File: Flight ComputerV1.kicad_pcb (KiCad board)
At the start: 4 copper layers, 100 x 100 mm, 37 parts, among them J101 ICSP, J102 Screw_Terminal_01x02, J103 Conn_01x08, J104 Conn_01x07, J105 Micro_SD_Card, J106 Conn_02x10_Top_Bottom, J201 Conn_Coaxial, SW101 1-1825910-8, U101 ATmega328PB-A, U102 LMT84DCK, U201 RXM-GPS-RM-T, U301 LIS3MDLTR, U302 LSM6DSOXTR

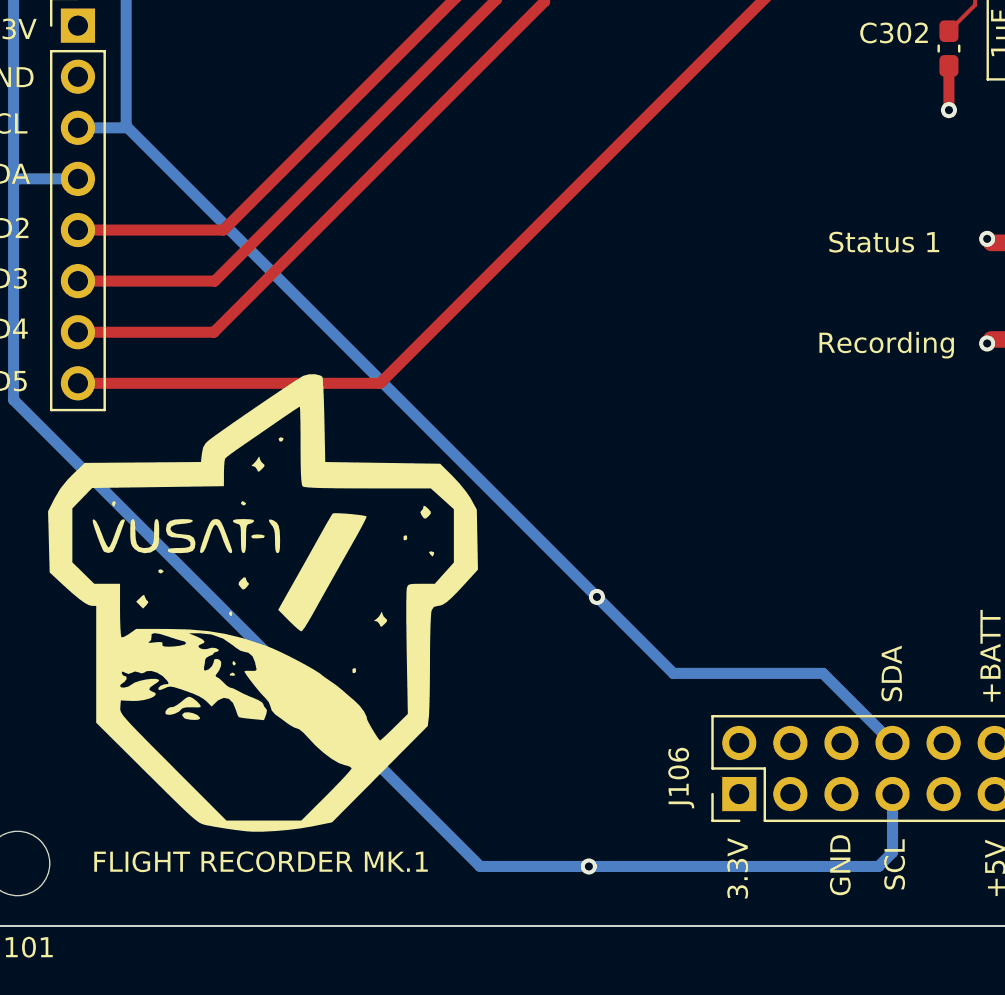
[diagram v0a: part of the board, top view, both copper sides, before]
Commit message: Updated pull-up resistors
Added pull-up resistors and testing github.
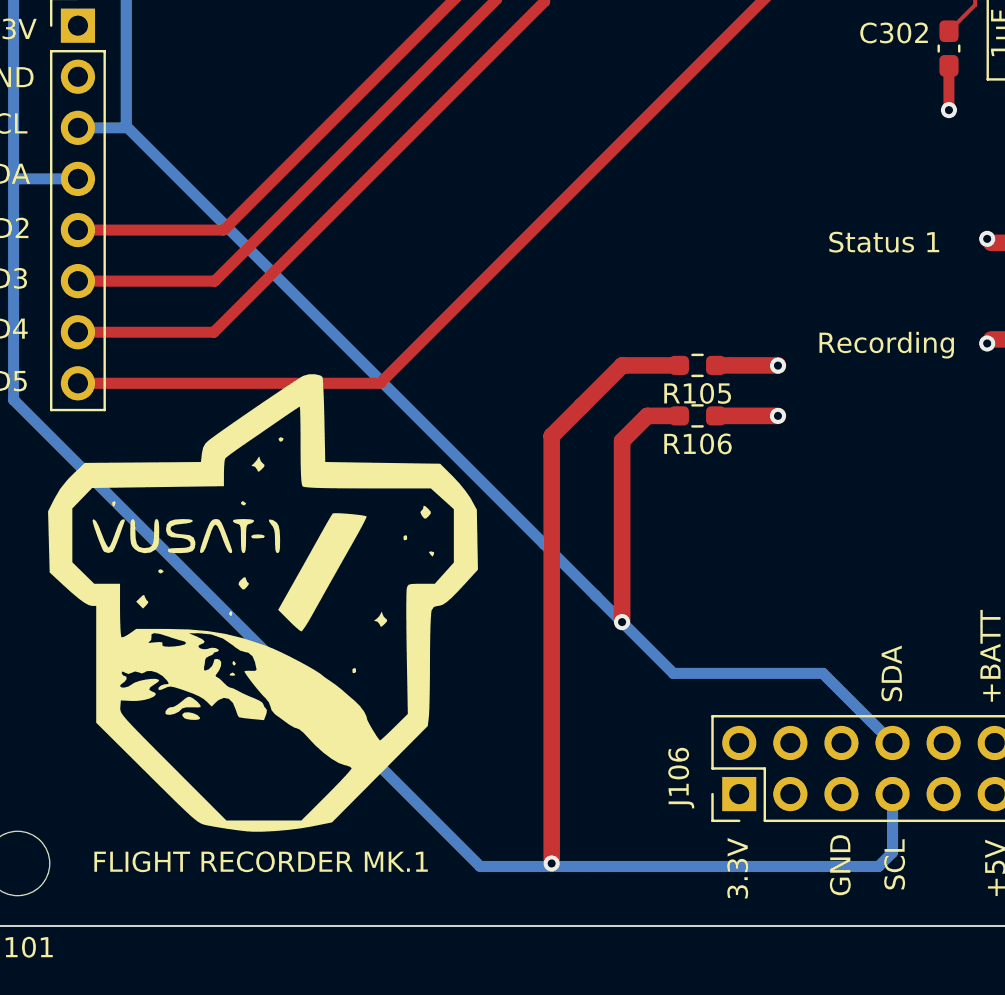
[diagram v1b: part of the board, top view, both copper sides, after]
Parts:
- added R105: 2.2K, Resistor_SMD:R_0603_1608Metric_Pad0.98x0.95mm_HandSolder, F.Cu at (208.0, 148.5)
- added R106: 2.2K, Resistor_SMD:R_0603_1608Metric_Pad0.98x0.95mm_HandSolder, F.Cu at (208.0, 151.0)
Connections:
- D102 pad 1: GND -> unconnected-(D102-Pad1)
- U101 pad 17: /SCLK -> unconnected-(U101-Pad17)
- U101 pad 21: GND -> Net-(U101-Pad21)
- U101 pad 23: /MISO1 -> unconnected-(U101-Pad23)
- U101 pad 24: /SCK1 -> unconnected-(U101-Pad24)
- U101 pad 25: /T_OUT1 -> unconnected-(U101-Pad25)
- U101 pad 26: /INT_IMU -> unconnected-(U101-Pad26)
- U101 pad 27: /PC4 -> unconnected-(U101-Pad27)
- U101 pad 28: /PC5 -> unconnected-(U101-Pad28)
- U101 pad 29: /RST -> unconnected-(U101-Pad29)
- U101 pad 5: GND -> Net-(U101-Pad21)
- U301 pad 7: /INT_MAG -> /IMU/INT_MAG
- U301 pad 8: /DRDY -> /IMU/DRDY
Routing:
- net unconnected-(U101-Pad28): track 0.00 -> 60.4 mm, vias 0 -> 2
- net /PC5: track 60.4 -> 0.00 mm, vias 2 -> 0
- net SDA: track 243.7 -> 272.8 mm
- net SCL: track 199.0 -> 211.4 mm
- net GND: track 76.0 -> 64.9 mm, vias 28 -> 25
- net /IMU/DRDY: track 0.00 -> 10.4 mm
- net /DRDY: track 10.4 -> 0.00 mm
- net Net-(U101-Pad21): track 0.00 -> 8.81 mm, vias 0 -> 2
- net +3V3: track 43.3 -> 49.5 mm, vias 8 -> 10
- net unconnected-(D102-Pad1): track 0.00 -> 2.23 mm, vias 0 -> 1

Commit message: 10/18 changes
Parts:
- added MISO: MISO, TestPoint:TestPoint_Pad_1.5x1.5mm, F.Cu at (243.8, 118.7)
- added MISO1: MISO1, TestPoint:TestPoint_Pad_1.5x1.5mm, F.Cu at (237.5, 104.8)
- added MOSI: MOSI, TestPoint:TestPoint_Pad_1.5x1.5mm, F.Cu at (248.3, 118.7)
- added MOSI1: MOSI1, TestPoint:TestPoint_Pad_1.5x1.5mm, F.Cu at (233.2, 104.8)
- added SCK1: SCK1, TestPoint:TestPoint_Pad_1.5x1.5mm, F.Cu at (241.6, 104.6)
- added SCLK: SCLK, TestPoint:TestPoint_Pad_1.5x1.5mm, F.Cu at (239.3, 118.9)
- added TP 3.3V: TestPoint_Pad_1.5x1.5mm, TestPoint:TestPoint_Pad_1.5x1.5mm, F.Cu at (210.7, 92.5)
- added TP GND: TestPoint_Pad_1.5x1.5mm, TestPoint:TestPoint_Pad_1.5x1.5mm, F.Cu at (217.3, 92.5)
- added TP RX: TestPoint_Pad_1.5x1.5mm, TestPoint:TestPoint_Pad_1.5x1.5mm, F.Cu at (196.2, 101.6)
- added TP SCL: TestPoint_Pad_1.5x1.5mm, TestPoint:TestPoint_Pad_1.5x1.5mm, F.Cu at (249.4, 94.4)
- added TP SDA: TestPoint_Pad_1.5x1.5mm, TestPoint:TestPoint_Pad_1.5x1.5mm, F.Cu at (245.0, 94.5)
- added TP TX: TestPoint_Pad_1.5x1.5mm, TestPoint:TestPoint_Pad_1.5x1.5mm, F.Cu at (191.3, 101.6)
- added TP10: TX, TestPoint:TestPoint_Pad_1.5x1.5mm, F.Cu at (203.8, 139.5)
- added TP11: GND, TestPoint:TestPoint_Pad_1.5x1.5mm, F.Cu at (207.4, 135.9)
- added TP12: 3.3V, TestPoint:TestPoint_Pad_1.5x1.5mm, F.Cu at (200.3, 139.5)
- added TP7: SDA, TestPoint:TestPoint_Pad_1.5x1.5mm, F.Cu at (203.8, 143.0)
- added TP8: SCL, TestPoint:TestPoint_Pad_1.5x1.5mm, F.Cu at (210.9, 135.9)
- added TP9: RX, TestPoint:TestPoint_Pad_1.5x1.5mm, F.Cu at (196.7, 135.9)
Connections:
- C101 pad 2: 3.3V -> +3V3
- R101 pad 2: 3.3V -> +3V3
- U101 pad 17: unconnected-(U101-Pad17) -> /SCLK
- U101 pad 18: 3.3V -> +3V3
- U101 pad 20: 3.3V -> +3V3
- U101 pad 21: Net-(U101-Pad21) -> GND
- U101 pad 4: 3.3V -> +3V3
- U101 pad 5: Net-(U101-Pad21) -> GND
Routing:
- net unconnected-(U101-Pad27): track 0.00 -> 60.9 mm, vias 0 -> 2
- net /PC4: track 60.9 -> 0.00 mm, vias 2 -> 0
- net +3V3: track 49.5 -> 67.4 mm, vias 10 -> 13
- net 3.3V: track 17.8 -> 2.97 mm, vias 2 -> 0
- net GND: track 64.9 -> 76.7 mm, vias 25 -> 29
- net /INT_MAG: track 11.2 -> 0.00 mm
- net /IMU/INT_MAG: track 0.00 -> 11.2 mm
- net /MOSI1: track 25.7 -> 36.6 mm, vias 0 -> 2
- net SCL: track 211.4 -> 220.7 mm, vias 4 -> 5
- net Net-(U101-Pad21): track 8.81 -> 0.00 mm, vias 2 -> 0
- net /SCLK: track 81.5 -> 90.3 mm
- net /SCK1: track 27.5 -> 36.0 mm, vias 0 -> 2
- net /MISO1: track 28.4 -> 36.8 mm, vias 0 -> 2
- net /MOSI: track 78.0 -> 86.1 mm, vias 1 -> 3
- net SDA: track 272.8 -> 278.3 mm, vias 5 -> 6
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- added copper zone on In2.Cu, net +3V3
- removed copper zone on In2.Cu, net 3.3V
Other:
- board text added: "+"
- board text added: "-"
- board text added: "Class of 2026"

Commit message: 10/19 Updated Files
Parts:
- removed TP 3.3V: TestPoint_Pad_1.5x1.5mm, TestPoint:TestPoint_Pad_1.5x1.5mm
- removed TP GND: TestPoint_Pad_1.5x1.5mm, TestPoint:TestPoint_Pad_1.5x1.5mm
- removed TP RX: TestPoint_Pad_1.5x1.5mm, TestPoint:TestPoint_Pad_1.5x1.5mm
- removed TP SCL: TestPoint_Pad_1.5x1.5mm, TestPoint:TestPoint_Pad_1.5x1.5mm
- removed TP SDA: TestPoint_Pad_1.5x1.5mm, TestPoint:TestPoint_Pad_1.5x1.5mm
- removed TP TX: TestPoint_Pad_1.5x1.5mm, TestPoint:TestPoint_Pad_1.5x1.5mm
- moved TP7 64.3 mm to (245.4, 94.0)
- moved TP8 56.9 mm to (249.4, 94.0)
- moved TP12 48.7 mm to (210.8, 91.9)
- moved TP11 45.1 mm to (217.4, 91.9)
- moved TP10 41.1 mm to (190.5, 100.6)
- moved TP9 35.3 mm to (196.1, 100.6)
- renumbered MOSI to TP1, MISO to TP2, SCLK to TP3, SCK1 to TP4, MISO1 to TP5, MOSI1 to TP6
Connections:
- D102 pad 1: unconnected-(D102-Pad1) -> GND
- U101 pad 23: unconnected-(U101-Pad23) -> /MISO1
- U101 pad 24: unconnected-(U101-Pad24) -> /SCK1
- U101 pad 25: unconnected-(U101-Pad25) -> Net-(C105-Pad1)
- U101 pad 26: unconnected-(U101-Pad26) -> /INT_IMU
- U101 pad 27: unconnected-(U101-Pad27) -> /PC4
- U101 pad 28: unconnected-(U101-Pad28) -> /PC5
- U201 pad 20: unconnected-(U201-Pad20) -> GND
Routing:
- net unconnected-(U101-Pad27): track 60.9 -> 0.00 mm, vias 2 -> 0
- net /PC4: track 0.00 -> 60.9 mm, vias 0 -> 2
- net unconnected-(U101-Pad28): track 60.4 -> 0.00 mm, vias 2 -> 0
- net /PC5: track 0.00 -> 60.4 mm, vias 0 -> 2
- net /INT_MAG: track 0.00 -> 11.2 mm
- net /IMU/INT_MAG: track 11.2 -> 0.00 mm
- net /IMU/DRDY: track 10.4 -> 0.00 mm
- net /DRDY: track 0.00 -> 10.4 mm
- net GND: track 76.7 -> 82.9 mm, vias 29 -> 30
- net +3V3: track 67.4 -> 72.1 mm
- net unconnected-(U201-Pad20): track 3.36 -> 0.00 mm, vias 1 -> 0
- net 3.3V: track 2.97 -> 0.00 mm
- net unconnected-(D102-Pad1): track 2.24 -> 0.00 mm
- net TX: track 69.4 -> 71.2 mm
- net RX: track 66.4 -> 67.6 mm
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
